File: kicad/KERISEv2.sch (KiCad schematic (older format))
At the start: 11 parts, among them SW1 RESET, U1 STM32F405RGTx

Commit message: 新基板，部品を配置
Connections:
- net LED_5: now reaches U1.40 (PC9/DAC_EXTI9/I2C3_SDA/I2S_CKIN/RCC_MCO_2/SDIO_D1/TIM3_CH4/TIM8_CH4)
- net LED_6: now reaches U1.51 (PC10/I2S3_CK/SDIO_D2/SPI3_SCK/UART4_TX/USART3_TX)
- no-connect marks 22 -> 20
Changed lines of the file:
@@
 AXIS_INT
 $Sheet
-S 1300 2000 1000 500
+S 1300 2000 1000 700
 U 57CD8D81
 F0 "UI" 60
@@
 F6 "LED_4" I L 1300 2400 60
 F7 "BUTTON" I R 2300 2200 60
+F8 "LED_5" I L 1300 2500 60
+F9 "LED_6" I L 1300 2600 60
 $EndSheet
 $Sheet
@@
 NoConn ~ 10300 3700
 NoConn ~ 10300 3800
-NoConn ~ 10300 5100
-NoConn ~ 10300 5200
 NoConn ~ 10300 5300
 NoConn ~ 10300 5400
@@
 F1 "Charger.sch" 60
 $EndSheet
+Text GLabel 1200 2500 0    50   Input ~ 0
+LED_5
+Text GLabel 1200 2600 0    50   Input ~ 0
+LED_6
+Wire Wire Line
+	1200 2600 1300 2600
+Wire Wire Line
+	1300 2500 1200 2500
+Text GLabel 10400 5100 2    50   Input ~ 0
+LED_5
+Text GLabel 10400 5200 2    50   Input ~ 0
+LED_6
+Wire Wire Line
+	10400 5100 10300 5100
+Wire Wire Line
+	10300 5200 10400 5200
 $EndSCHEMATC

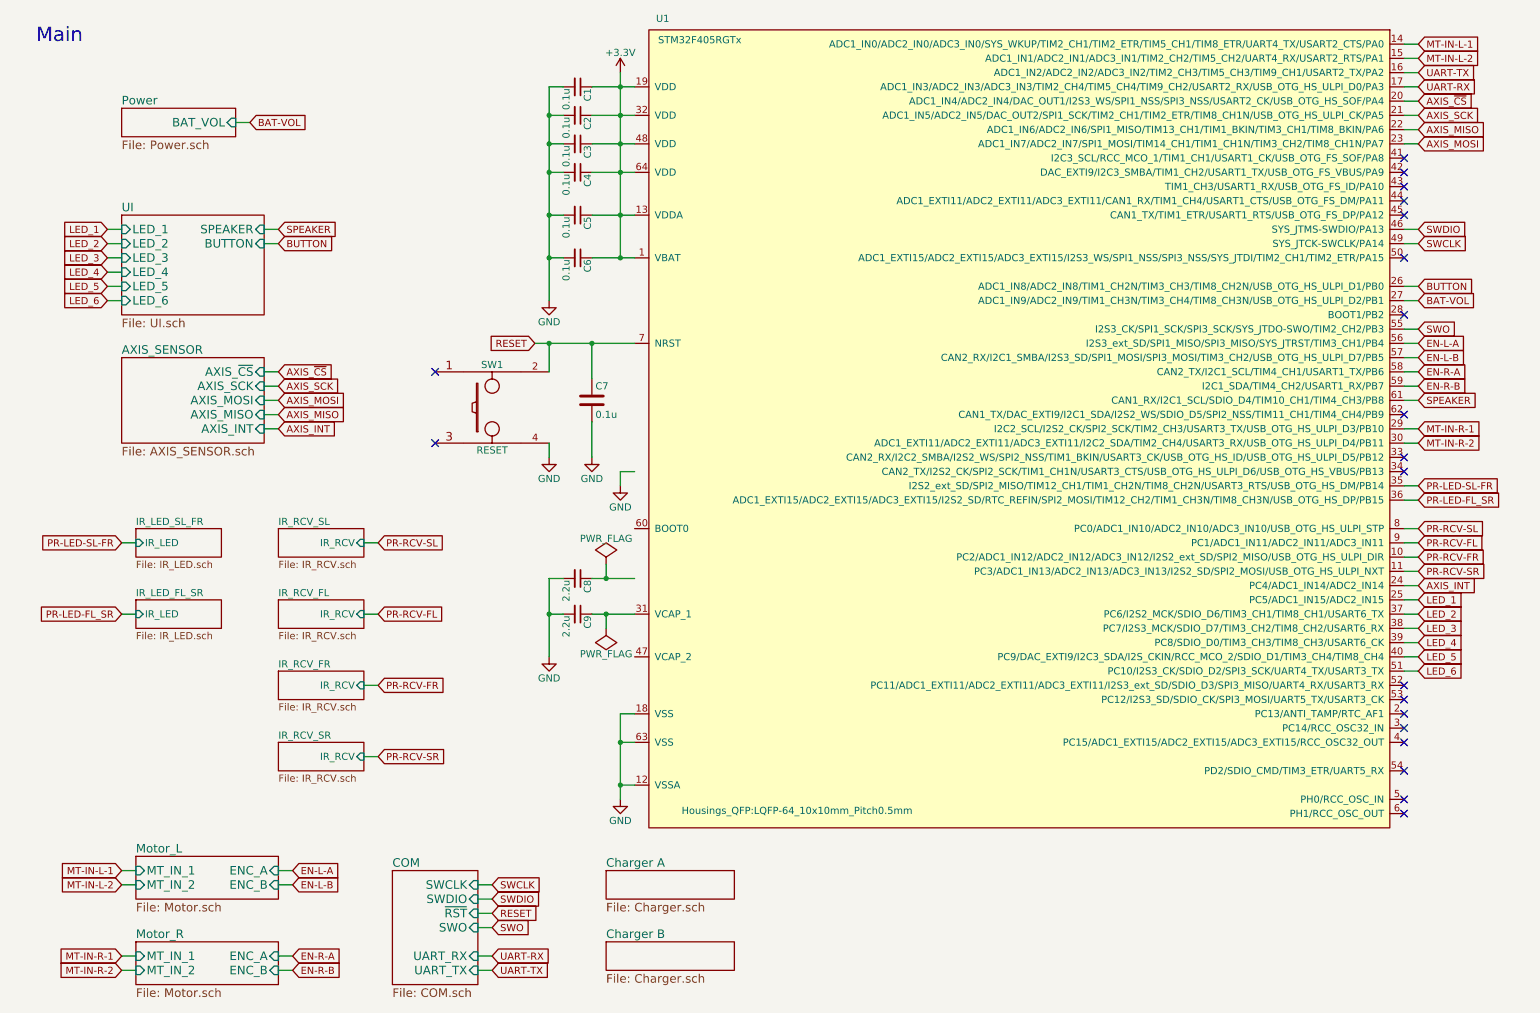
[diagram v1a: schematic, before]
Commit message: 自動配線用にdsn吐き出し
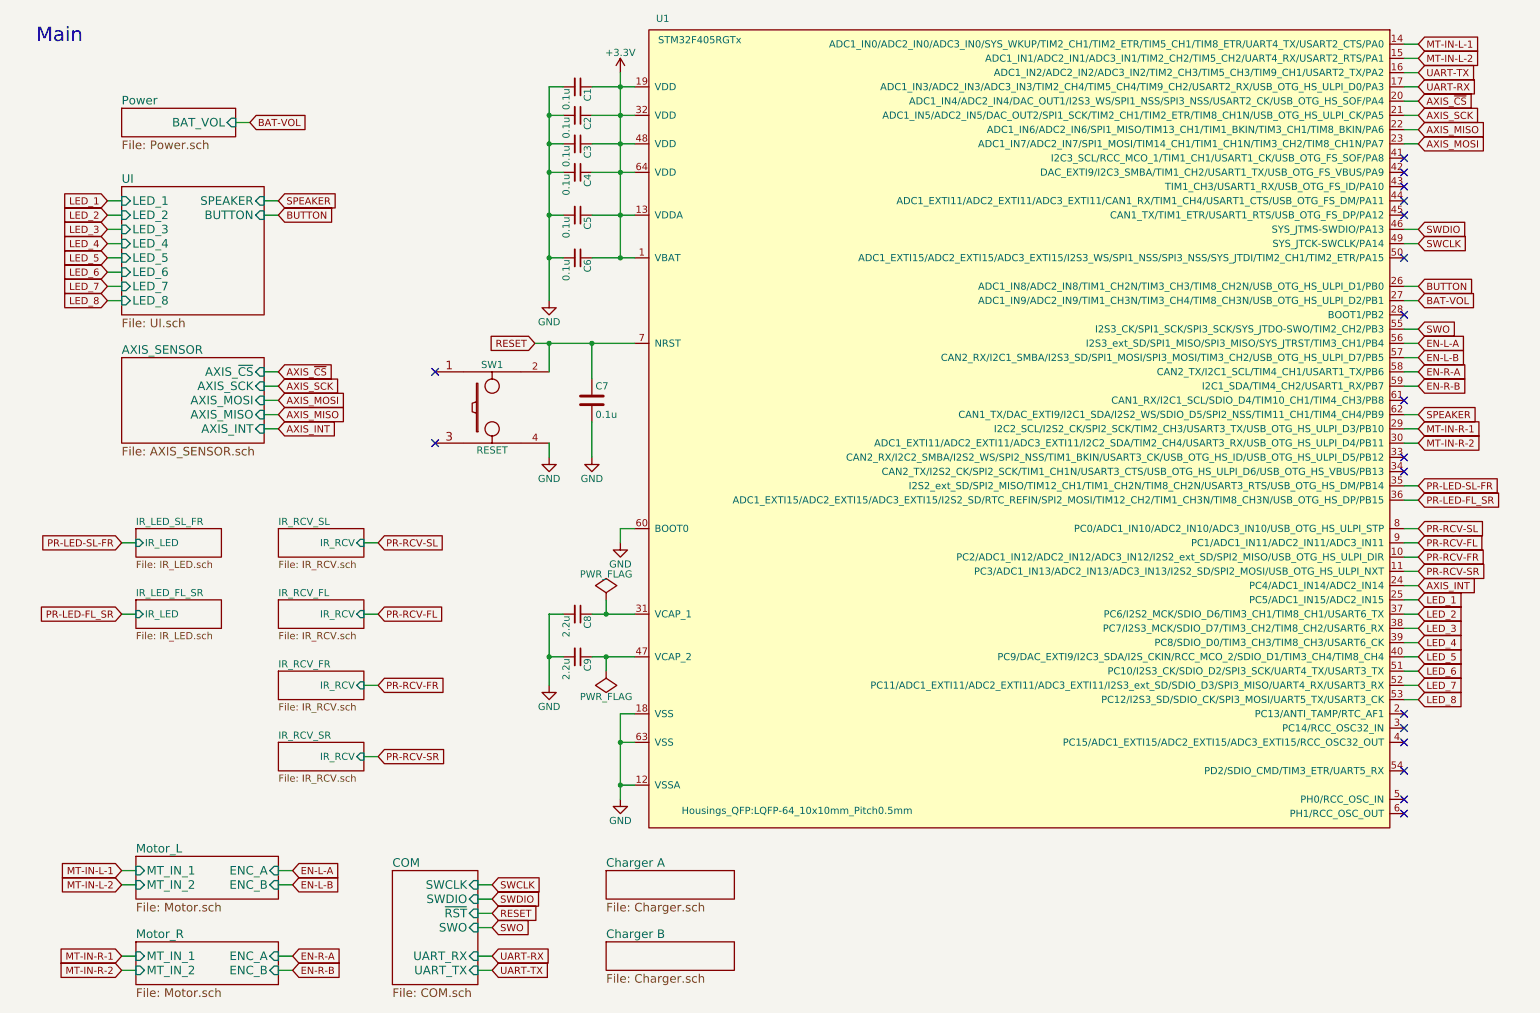
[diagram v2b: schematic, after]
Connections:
- net GND: now also U1.60 (BOOT0)
- net SPEAKER: now also U1.62 (CAN1_TX/DAC_EXTI9/I2C1_SDA/I2S2_WS/SDIO_D5/SPI2_NSS/TIM11_CH1/TIM4_CH4/PB9); no longer U1.61 (CAN1_RX/I2C1_SCL/SDIO_D4/TIM10_CH1/TIM4_CH3/PB8)
- net at U1.31 (VCAP_1): now also C8.1; no longer C9.1
- net at U1.47 (VCAP_2): now also C9.1
- net LED_7: now reaches U1.52 (PC11/ADC1_EXTI11/ADC2_EXTI11/ADC3_EXTI11/I2S3_ext_SD/SDIO_D3/SPI3_MISO/UART4_RX/USART3_RX)
- net LED_8: now reaches U1.53 (PC12/I2S3_SD/SDIO_CK/SPI3_MOSI/UART5_TX/USART3_CK)
- no-connect marks 20 -> 18
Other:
- moved on the sheet: C8, C9
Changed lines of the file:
@@
 L C_Small C9
 U 1 1 57C91C59
+P 4500 5100
+F 0 "C9" H 4510 5170 50  0000 L CNN
+F 1 "2.2u" H 4510 5020 50  0000 L CNN
+F 2 "Capacitors_SMD:C_0603" H 4500 5100 50  0001 C CNN
+F 3 "" H 4500 5100 50  0000 C CNN
+	1    4500 5100
+	0    1    1    0
+$EndComp
+$Comp
+L C_Small C8
+U 1 1 57C928EA
 P 4500 4800
-F 0 "C9" H 4510 4870 50  0000 L CNN
+F 0 "C8" H 4510 4870 50  0000 L CNN
 F 1 "2.2u" H 4510 4720 50  0000 L CNN
 F 2 "Capacitors_SMD:C_0603" H 4500 4800 50  0001 C CNN
 F 3 "" H 4500 4800 50  0000 C CNN
 	1    4500 4800
-	0    1    1    0
-$EndComp
-$Comp
-L C_Small C8
-U 1 1 57C928EA
-P 4500 4550
-F 0 "C8" H 4510 4620 50  0000 L CNN
-F 1 "2.2u" H 4510 4470 50  0000 L CNN
-F 2 "Capacitors_SMD:C_0603" H 4500 4550 50  0001 C CNN
-F 3 "" H 4500 4550 50  0000 C CNN
-	1    4500 4550
 	0    1    1    0
 $EndComp
@@
 L GND #PWR04
 U 1 1 57C99E1F
-P 4300 5100
-F 0 "#PWR04" H 4300 4850 50  0001 C CNN
-F 1 "GND" H 4300 4950 50  0000 C CNN
-F 2 "" H 4300 5100 50  0000 C CNN
-F 3 "" H 4300 5100 50  0000 C CNN
-	1    4300 5100
+P 4300 5300
+F 0 "#PWR04" H 4300 5050 50  0001 C CNN
+F 1 "GND" H 4300 5150 50  0000 C CNN
+F 2 "" H 4300 5300 50  0000 C CNN
+F 3 "" H 4300 5300 50  0000 C CNN
+	1    4300 5300
 	1    0    0    -1
 $EndComp
@@
 F 3 "" H 4800 6100 50  0000 C CNN
 	1    4800 6100
-	1    0    0    -1
-$EndComp
-$Comp
-L GND #PWR06
-U 1 1 57CA25EF
-P 4800 3900
-F 0 "#PWR06" H 4800 3650 50  0001 C CNN
-F 1 "GND" H 4800 3750 50  0000 C CNN
-F 2 "" H 4800 3900 50  0000 C CNN
-F 3 "" H 4800 3900 50  0000 C CNN
-	1    4800 3900
 	1    0    0    -1
 $EndComp
@@
 $EndComp
 $Comp
-L GND #PWR07
+L GND #PWR06
 U 1 1 57CDA895
 P 4300 2600
-F 0 "#PWR07" H 4300 2350 50  0001 C CNN
+F 0 "#PWR06" H 4300 2350 50  0001 C CNN
 F 1 "GND" H 4300 2450 50  0000 C CNN
 F 2 "" H 4300 2600 50  0000 C CNN
@@
 AXIS_INT
 $Sheet
-S 1300 2000 1000 700
+S 1300 1800 1000 900
 U 57CD8D81
 F0 "UI" 60
 F1 "UI.sch" 60
-F2 "SPEAKER" I R 2300 2100 60
-F3 "LED_1" I L 1300 2100 60
-F4 "LED_2" I L 1300 2200 60
-F5 "LED_3" I L 1300 2300 60
-F6 "LED_4" I L 1300 2400 60
-F7 "BUTTON" I R 2300 2200 60
-F8 "LED_5" I L 1300 2500 60
-F9 "LED_6" I L 1300 2600 60
+F2 "SPEAKER" I R 2300 1900 60
+F3 "LED_1" I L 1300 1900 60
+F4 "LED_2" I L 1300 2000 60
+F5 "LED_3" I L 1300 2100 60
+F6 "LED_4" I L 1300 2200 60
+F7 "BUTTON" I R 2300 2000 60
+F8 "LED_5" I L 1300 2300 60
+F9 "LED_6" I L 1300 2400 60
+F10 "LED_7" I L 1300 2500 60
+F11 "LED_8" I L 1300 2600 60
 $EndSheet
 $Sheet
@@
 Text GLabel 10400 1000 2    50   Input ~ 0
 UART-TX
+Text GLabel 1200 1900 0    50   Input ~ 0
+LED_1
+Text GLabel 1200 2000 0    50   Input ~ 0
+LED_2
 Text GLabel 1200 2100 0    50   Input ~ 0
-LED_1
+LED_3
 Text GLabel 1200 2200 0    50   Input ~ 0
-LED_2
-Text GLabel 1200 2300 0    50   Input ~ 0
-LED_3
-Text GLabel 1200 2400 0    50   Input ~ 0
 LED_4
-Text GLabel 2400 2200 2    50   Input ~ 0
+Text GLabel 2400 2000 2    50   Input ~ 0
 BUTTON
-Text GLabel 2400 2100 2    50   Input ~ 0
+Text GLabel 2400 1900 2    50   Input ~ 0
 SPEAKER
 Text GLabel 10400 4700 2    50   Input ~ 0
@@
 Text GLabel 10400 2500 2    50   Input ~ 0
 BUTTON
-Text GLabel 10400 3300 2    50   Input ~ 0
+Text GLabel 10400 3400 2    50   Input ~ 0
 SPEAKER
 $Comp
+L PWR_FLAG #FLG07
+U 1 1 57D09A39
+P 4700 4700
+F 0 "#FLG07" H 4700 4795 50  0001 C CNN
+F 1 "PWR_FLAG" H 4700 4880 50  0000 C CNN
+F 2 "" H 4700 4700 50  0000 C CNN
+F 3 "" H 4700 4700 50  0000 C CNN
+	1    4700 4700
+	1    0    0    -1
+$EndComp
+$Comp
 L PWR_FLAG #FLG08
-U 1 1 57D09A39
-P 4700 4450
-F 0 "#FLG08" H 4700 4545 50  0001 C CNN
-F 1 "PWR_FLAG" H 4700 4630 50  0000 C CNN
-F 2 "" H 4700 4450 50  0000 C CNN
-F 3 "" H 4700 4450 50  0000 C CNN
-	1    4700 4450
-	1    0    0    -1
-$EndComp
-$Comp
-L PWR_FLAG #FLG09
 U 1 1 57D180C1
-P 4700 4900
-F 0 "#FLG09" H 4700 4995 50  0001 C CNN
-F 1 "PWR_FLAG" H 4700 5080 50  0000 C CNN
-F 2 "" H 4700 4900 50  0000 C CNN
-F 3 "" H 4700 4900 50  0000 C CNN
-	1    4700 4900
+P 4700 5200
+F 0 "#FLG08" H 4700 5295 50  0001 C CNN
+F 1 "PWR_FLAG" H 4700 5380 50  0000 C CNN
+F 2 "" H 4700 5200 50  0000 C CNN
+F 3 "" H 4700 5200 50  0000 C CNN
+	1    4700 5200
 	-1   0    0    1
 $EndComp
@@
 NoConn ~ 10300 3700
 NoConn ~ 10300 3800
-NoConn ~ 10300 5300
-NoConn ~ 10300 5400
 NoConn ~ 10300 5500
 NoConn ~ 10300 5600
@@
 Text Notes 700  800  0    100  ~ 0
 Main
-NoConn ~ 10300 3400
-NoConn ~ 10300 1700
-NoConn ~ 10300 1800
 $Comp
 L C_Small C1
@@
 	0    1    1    0
 $EndComp
+$Sheet
+S 4700 6600 900  200
+U 58401A83
+F0 "Charger A" 60
+F1 "Charger.sch" 60
+$EndSheet
+$Sheet
+S 4700 7100 900  200
+U 58410148
+F0 "Charger B" 60
+F1 "Charger.sch" 60
+$EndSheet
+Text GLabel 1200 2300 0    50   Input ~ 0
+LED_5
+Text GLabel 1200 2400 0    50   Input ~ 0
+LED_6
+Text GLabel 10400 5100 2    50   Input ~ 0
+LED_5
+Text GLabel 10400 5200 2    50   Input ~ 0
+LED_6
+Text GLabel 10400 5300 2    50   Input ~ 0
+LED_7
+Text GLabel 10400 5400 2    50   Input ~ 0
+LED_8
+$Comp
+L GND #PWR09
+U 1 1 58648E0B
+P 4800 4300
+F 0 "#PWR09" H 4800 4050 50  0001 C CNN
+F 1 "GND" H 4800 4150 50  0000 C CNN
+F 2 "" H 4800 4300 50  0000 C CNN
+F 3 "" H 4800 4300 50  0000 C CNN
+	1    4800 4300
+	1    0    0    -1
+$EndComp
 Wire Wire Line
 	4800 1000 4800 2300
@@
 	3800 6700 3900 6700
 Wire Wire Line
+	1200 1900 1300 1900
+Wire Wire Line
+	1300 2000 1200 2000
+Wire Wire Line
 	1200 2100 1300 2100
 Wire Wire Line
 	1300 2200 1200 2200
 Wire Wire Line
-	1200 2300 1300 2300
-Wire Wire Line
-	1300 2400 1200 2400
-Wire Wire Line
-	2400 2100 2300 2100
-Wire Wire Line
-	2300 2200 2400 2200
+	2400 1900 2300 1900
+Wire Wire Line
+	2300 2000 2400 2000
 Wire Wire Line
 	4200 2900 4900 2900
@@
 Connection ~ 4300 2900
 Wire Wire Line
-	4800 3900 4800 3800
-Wire Wire Line
-	4800 3800 4900 3800
-Wire Wire Line
-	4700 4450 4700 4550
-Wire Wire Line
-	4600 4550 4900 4550
-Wire Wire Line
-	4300 4550 4300 5100
-Wire Wire Line
-	4300 4800 4400 4800
-Wire Wire Line
-	4300 4550 4400 4550
-Connection ~ 4300 4800
-Connection ~ 4700 4550
-Wire Wire Line
-	4600 4800 4900 4800
-Wire Wire Line
-	4700 4800 4700 4900
-Connection ~ 4700 4800
-Wire Wire Line
 	10400 2200 10300 2200
 Wire Wire Line
@@
 	10300 4500 10400 4500
 Wire Wire Line
-	10400 1000 10300 1000
-Wire Wire Line
-	10300 1100 10400 1100
-Wire Wire Line
 	10400 3900 10300 3900
 Wire Wire Line
@@
 	10400 5000 10300 5000
 Wire Wire Line
-	10400 3300 10300 3300
-Wire Wire Line
 	10300 3200 10400 3200
 Wire Wire Line
@@
 Wire Wire Line
 	10300 1200 10400 1200
-Wire Wire Line
-	10400 3600 10300 3600
-Wire Wire Line
-	10300 3500 10400 3500
 Wire Wire Line
 	10400 900  10300 900
@@
 Wire Wire Line
 	4600 2300 4900 2300
+Wire Wire Line
+	1200 2400 1300 2400
+Wire Wire Line
+	1300 2300 1200 2300
+Wire Wire Line
+	10400 5100 10300 5100
+Wire Wire Line
+	10300 5200 10400 5200
+Wire Wire Line
+	4700 4700 4700 4800
+Wire Wire Line
+	4600 4800 4900 4800
+Connection ~ 4700 4800
+Wire Wire Line
+	4600 5100 4900 5100
+Wire Wire Line
+	4700 5100 4700 5200
+Connection ~ 4700 5100
+Wire Wire Line
+	4300 4800 4300 5300
+Wire Wire Line
+	4300 5100 4400 5100
+Wire Wire Line
+	4300 4800 4400 4800
+Connection ~ 4300 5100
+Wire Wire Line
+	4800 4300 4800 4200
+Wire Wire Line
+	4800 4200 4900 4200
+Wire Wire Line
+	10400 5300 10300 5300
+Wire Wire Line
+	10300 5400 10400 5400
+Wire Wire Line
+	10400 3400 10300 3400
+NoConn ~ 10300 3300
+Wire Wire Line
+	10400 3500 10300 3500
+Wire Wire Line
+	10300 3600 10400 3600
 $Comp
 L C_Small C6
@@
 	0    1    1    0
 $EndComp
-$Sheet
-S 4700 6600 900  200
-U 58401A83
-F0 "Charger A" 60
-F1 "Charger.sch" 60
-$EndSheet
-$Sheet
-S 4700 7100 900  200
-U 58410148
-F0 "Charger B" 60
-F1 "Charger.sch" 60
-$EndSheet
 Text GLabel 1200 2500 0    50   Input ~ 0
-LED_5
+LED_7
 Text GLabel 1200 2600 0    50   Input ~ 0
-LED_6
+LED_8
 Wire Wire Line
 	1200 2600 1300 2600
 Wire Wire Line
 	1300 2500 1200 2500
-Text GLabel 10400 5100 2    50   Input ~ 0
-LED_5
-Text GLabel 10400 5200 2    50   Input ~ 0
-LED_6
-Wire Wire Line
-	10400 5100 10300 5100
-Wire Wire Line
-	10300 5200 10400 5200
+NoConn ~ 10300 1800
+NoConn ~ 10300 1700
+Wire Wire Line
+	10400 1100 10300 1100
+Wire Wire Line
+	10300 1000 10400 1000
 $EndSCHEMATC
